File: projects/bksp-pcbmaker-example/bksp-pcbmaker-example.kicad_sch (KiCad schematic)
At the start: 2 parts

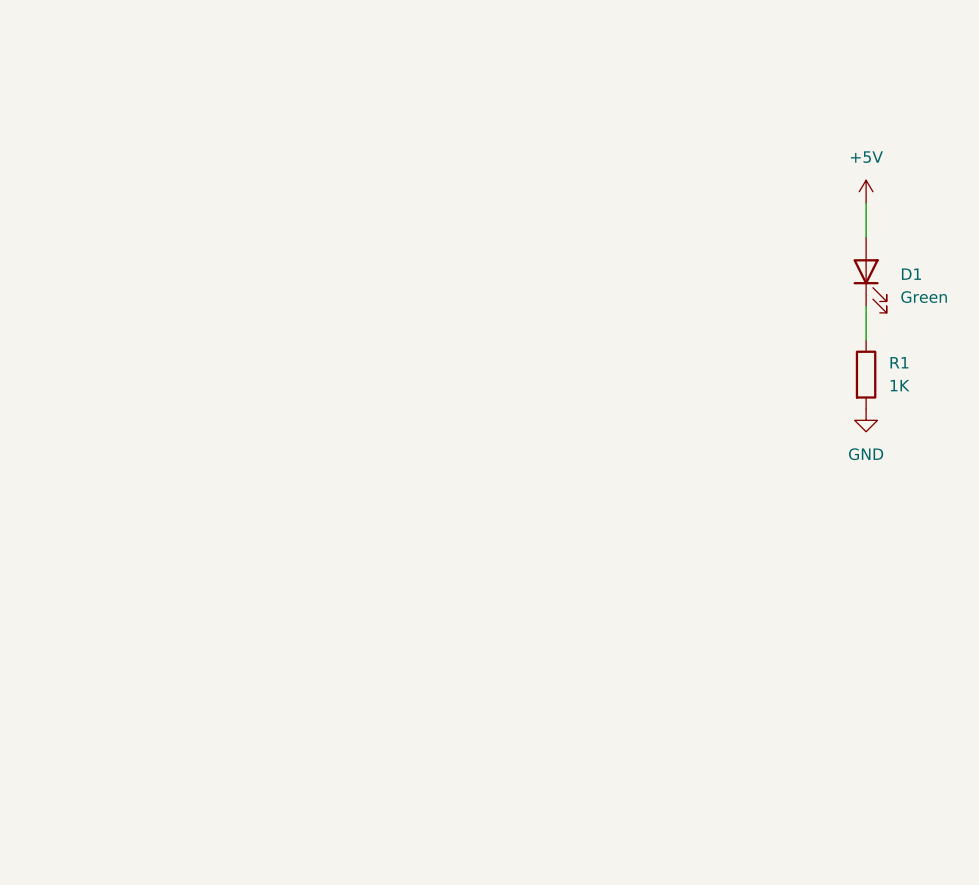
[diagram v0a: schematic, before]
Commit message: feat(reference): update DRC & Copper Fill settings in a reference project
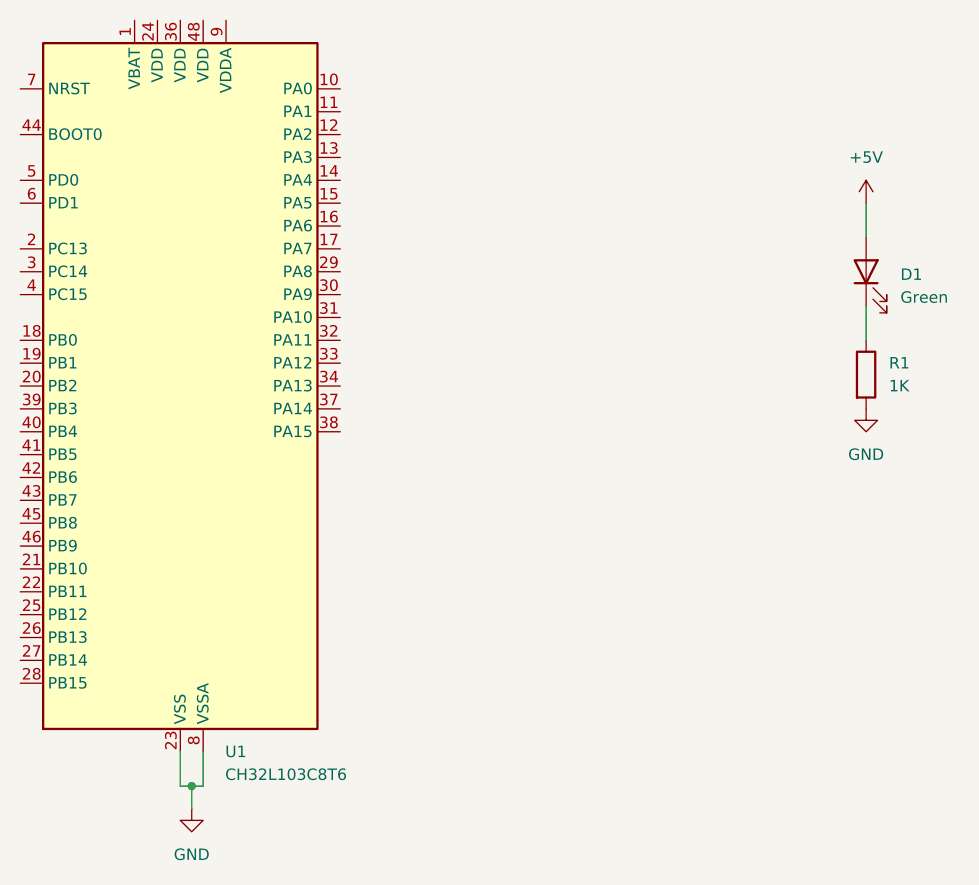
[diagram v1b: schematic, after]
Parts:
- added U1: CH32L103C8T6, Package_QFP:LQFP-48_7x7mm_P0.5mm, symbol BKSP:MCU_CH32L103C8T6
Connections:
- net GND: now also U1.23 (VSS), U1.35 (VSS), U1.47 (VSS), U1.8 (VSSA)
